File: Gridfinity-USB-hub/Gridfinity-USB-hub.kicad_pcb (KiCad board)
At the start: 4 copper layers, 40 x 40 mm, 38 parts, among them J1 USB_C_Receptacle_USB2.0_16P, J2 QWIIC, J3 USB_C_Receptacle_USB2.0_16P, J4 USB_C_Receptacle_USB2.0_16P, J5 USB_C_Receptacle_USB2.0_16P, J6 USB_C_Receptacle_USB2.0_16P, U1 CH334F, Y1 12MHz

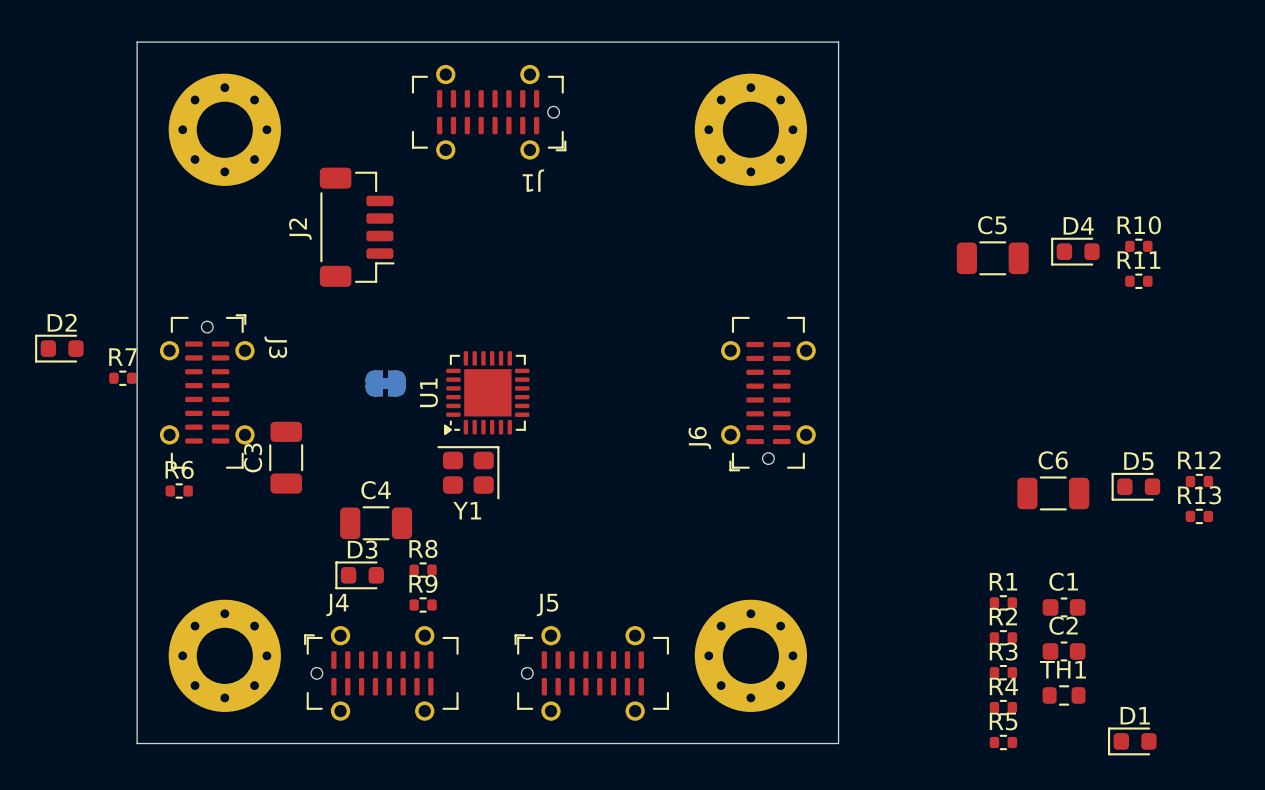
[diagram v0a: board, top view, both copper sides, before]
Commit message: USB Hub Board as order submitted on 9/6
This might get rejected by JLC for via sizes.
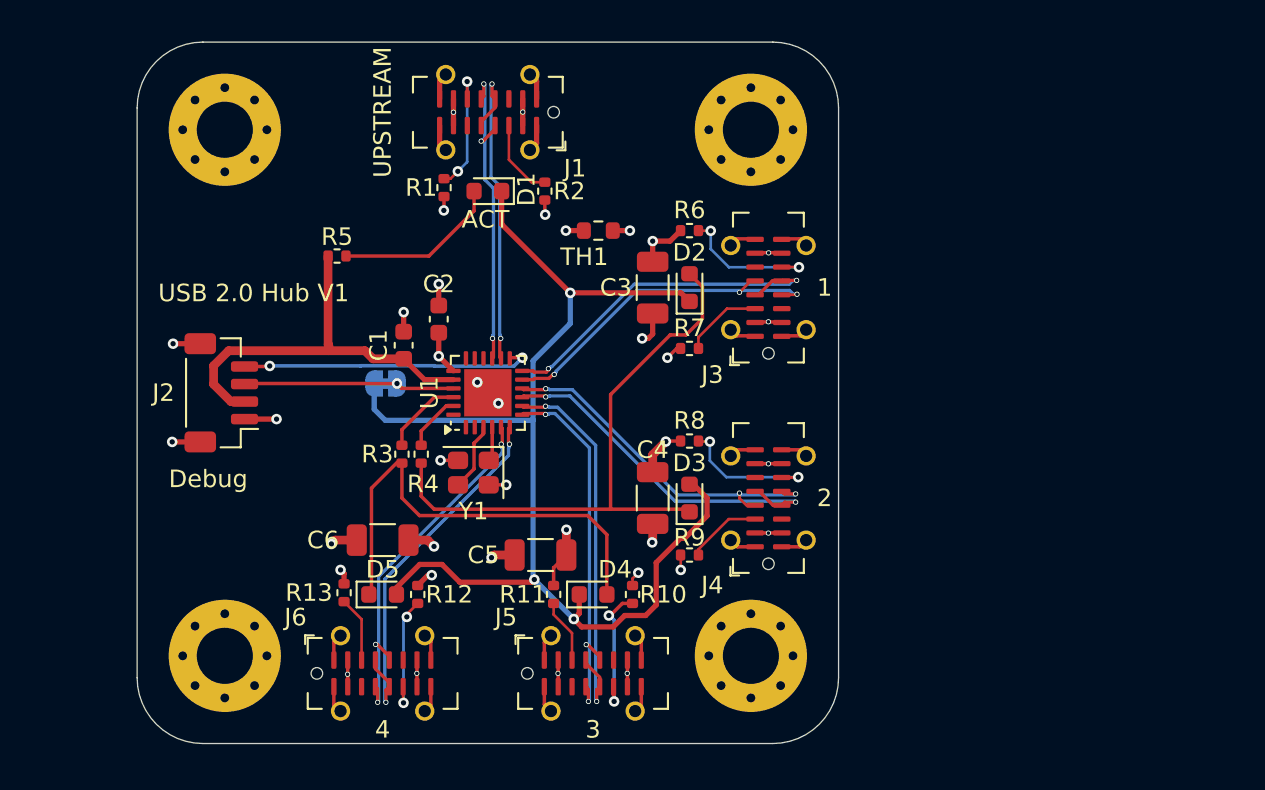
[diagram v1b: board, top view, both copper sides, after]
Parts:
- moved R13 49.0 mm to (61.8, 81.4), turned to -90 degrees
- moved D1 48.4 mm to (70.0, 58.5), turned to 180 degrees
- moved R5 47.0 mm to (61.4, 62.2)
- moved R12 45.0 mm to (66.0, 81.5), turned to -90 degrees
- moved D5 43.6 mm to (64.0, 81.5)
- moved C1 40.5 mm to (65.2, 67.3), turned to 90 degrees
- moved C2 40.4 mm to (67.2, 65.8), turned to 90 degrees
- moved R1 39.7 mm to (67.5, 58.3), turned to -90 degrees
- moved C6 38.3 mm to (64.0, 78.4), turned to 180 degrees
- moved R11 37.9 mm to (73.8, 81.5), turned to -90 degrees
- moved TH1 37.5 mm to (76.3, 60.8)
- moved R2 36.5 mm to (73.2, 58.5), turned to -90 degrees
- moved R3 36.5 mm to (65.1, 73.5), turned to -90 degrees
- moved R4 36.2 mm to (66.2, 73.5), turned to -90 degrees
- moved D2 35.9 mm to (81.5, 64.0), turned to 90 degrees
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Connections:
- J4 pad A6: /USB1.D+ -> /USB2.D+
- J4 pad A7: /USB1.D- -> /USB2.D-
- J4 pad B6: /USB1.D+ -> /USB2.D+
- J4 pad B7: /USB1.D- -> /USB2.D-
- J5 pad A6: /USB1.D+ -> /USB3.D+
- J5 pad A7: /USB1.D- -> /USB3.D-
- J5 pad B6: /USB1.D+ -> /USB3.D+
- J5 pad B7: /USB1.D- -> /USB3.D-
- J6 pad A6: /USB1.D+ -> /USB4.D+
- J6 pad A7: /USB1.D- -> /USB4.D-
- J6 pad B6: /USB1.D+ -> /USB4.D+
- J6 pad B7: /USB1.D- -> /USB4.D-
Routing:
- net /LED_COMMON: track 0.00 -> 70.6 mm, vias 0 -> 3
- net GND: track 0.00 -> 49.5 mm, vias 0 -> 15
- net /LED2: track 0.00 -> 34.0 mm
- net +5V: track 0.00 -> 28.9 mm, vias 0 -> 18
- net /LED1: track 0.00 -> 26.4 mm
- net +3V3: track 0.00 -> 23.4 mm
- net /USB3.D+: track 0.00 -> 22.6 mm, vias 0 -> 2
- net /USB3.D-: track 0.00 -> 21.5 mm, vias 0 -> 3
- net /USB4.D+: track 0.00 -> 21.5 mm, vias 0 -> 2
- net /USB4.D-: track 0.00 -> 21.1 mm, vias 0 -> 3
- net /USB2.D-: track 0.00 -> 20.9 mm, vias 0 -> 2
- net /USB1.D+: track 0.00 -> 20.6 mm, vias 0 -> 2
- net /USB2.D+: track 0.00 -> 20.4 mm, vias 0 -> 3
- net /USB1.D-: track 0.00 -> 20.0 mm, vias 0 -> 3
- net /Upstream.D-: track 0.00 -> 18.7 mm, vias 0 -> 2
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- added copper zone on In2.Cu, net VBUS
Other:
- outline, holes or cut-outs redrawn
- board text added: "1"
- board text added: "2"
- board text added: "3"
- board text added: "4"
- board text added: "ACT"
- board text added: "Debug"
- board text added: "SKEC ${ISSUE_DATE}"
- board text added: "UPSTREAM"
- board text added: "USB 2.0 Hub V${REVISION}"

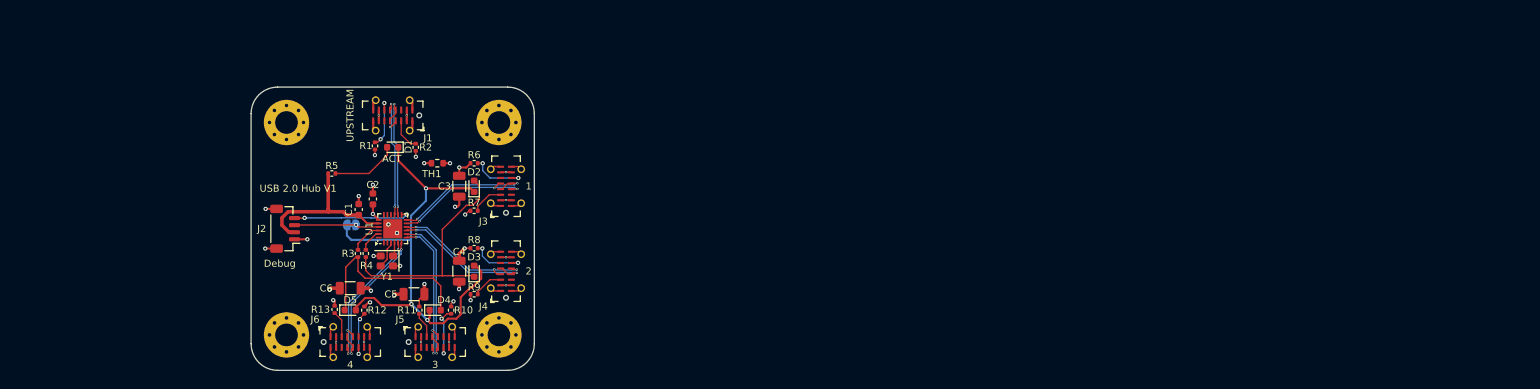
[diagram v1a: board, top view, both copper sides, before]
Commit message: Update to USB Hub to use symbol in library.  Probably some other changes as well
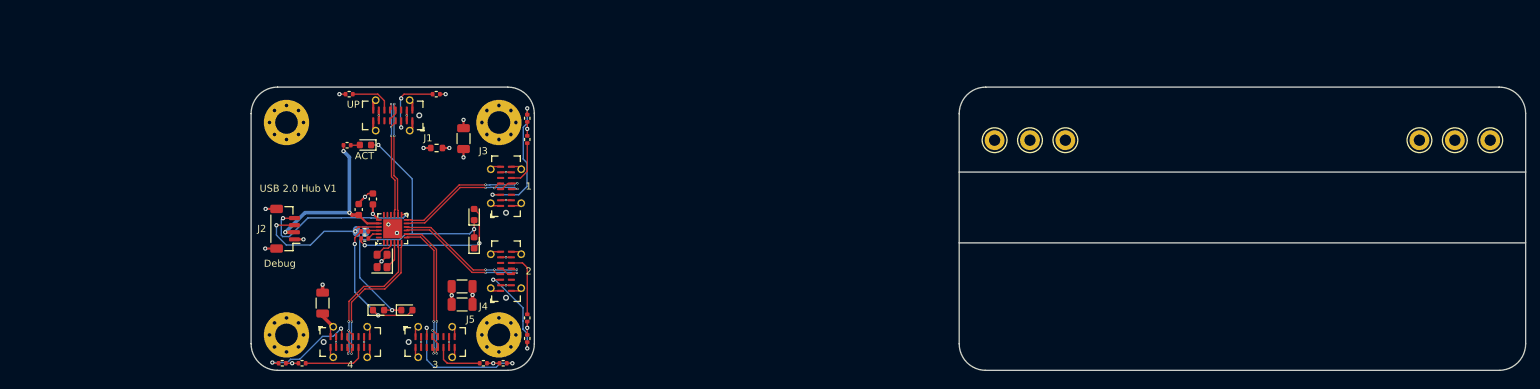
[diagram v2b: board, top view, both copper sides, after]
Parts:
- added REF**: TestPoint_Keystone_5010-5014_Multipurpose, TestPoint:TestPoint_Keystone_5010-5014_Multipurpose, F.Cu at (155.0, 57.5)
- added REF**: TestPoint_Keystone_5010-5014_Multipurpose, TestPoint:TestPoint_Keystone_5010-5014_Multipurpose, F.Cu at (220.0, 57.5)
- added REF**: TestPoint_Keystone_5010-5014_Multipurpose, TestPoint:TestPoint_Keystone_5010-5014_Multipurpose, F.Cu at (165.0, 57.5)
- added REF**: TestPoint_Keystone_5010-5014_Multipurpose, TestPoint:TestPoint_Keystone_5010-5014_Multipurpose, F.Cu at (215.0, 57.5)
- added REF**: TestPoint_Keystone_5010-5014_Multipurpose, TestPoint:TestPoint_Keystone_5010-5014_Multipurpose, F.Cu at (160.0, 57.5)
- added REF**: TestPoint_Keystone_5010-5014_Multipurpose, TestPoint:TestPoint_Keystone_5010-5014_Multipurpose, F.Cu at (225.0, 57.5)
- moved R7 15.1 mm to (89.0, 54.4), turned to 90 degrees
- moved R11 14.0 mm to (85.6, 89.0), turned to 0 degrees
- moved R8 12.4 mm to (89.0, 82.6), turned to 90 degrees
- moved R12 11.6 mm to (57.2, 89.0), turned to 0 degrees
- moved R13 10.6 mm to (54.4, 89.0), turned to 180 degrees
- moved R9 9.76 mm to (89.0, 85.5), turned to -90 degrees
- moved R10 8.77 mm to (82.8, 89.0), turned to 180 degrees
- moved R6 8.21 mm to (89.0, 57.4), turned to -90 degrees
- moved R1 8.16 mm to (63.9, 51.0), turned to 180 degrees
- moved R2 8.04 mm to (76.2, 51.0), turned to 0 degrees
- moved C5 6.95 mm to (79.8, 80.7)
- moved C3 6.75 mm to (80.0, 57.3)
- moved R5 4.54 mm to (63.6, 58.2)
- moved C6 4.43 mm to (60.1, 80.5), turned to -90 degrees
- moved D2 4.00 mm to (81.5, 68.0)
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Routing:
- net /LED_COMMON: track 70.6 -> 49.1 mm
- net Net-(J5-CC1): track 3.66 -> 19.3 mm, vias 0 -> 2
- net Net-(J3-CC1): track 4.55 -> 18.9 mm, vias 0 -> 2
- net /LED2: track 34.0 -> 23.7 mm, vias 0 -> 2
- net Net-(J6-CC1): track 3.74 -> 13.8 mm, vias 0 -> 2
- net Net-(J4-CC1): track 4.27 -> 13.8 mm, vias 0 -> 2
- net /SDA: track 12.0 -> 20.2 mm, vias 1 -> 2
- net Net-(D1-A): track 9.50 -> 1.31 mm
- net /SCL: track 16.8 -> 24.0 mm
- net /LED1: track 26.4 -> 19.8 mm, vias 0 -> 2
- net /CC1: track 4.53 -> 9.93 mm, vias 0 -> 2
- net +5V: track 28.9 -> 25.5 mm, vias 18 -> 16
- net Net-(U1-LED1): track 4.59 -> 1.53 mm
- net +3V3: track 23.4 -> 26.1 mm, vias 0 -> 3
- net Net-(J6-CC2): track 6.93 -> 9.27 mm, vias 2 -> 0
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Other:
- board size 40 x 40 mm -> 180 x 40 mm
- board text added: "2x Buss bar/power rail (Positive and Negative)"
- board text added: "5x30 Breadboard Grid"
- board text added: "Gnd"
- board text added: "Keystone 5010 (x2) & 5011 (x4) Electrically connected to the Power Rails"
- board text added: "Optional, but would fit in nicely with the Gridfinity standard"
- board text added: "Other connections to the 5x30 grid"
- board text added: "Pos"
- board text added: "UP"
- board text removed: "UPSTREAM"

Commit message: Checkpoint, changing computers
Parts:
- removed REF** (x6): TestPoint_Keystone_5010-5014_Multipurpose, TestPoint:TestPoint_Keystone_5010-5014_Multipurpose
- added C7: 10u, Capacitor_SMD:C_0603_1608Metric, F.Cu at (37.7, 69.4)
- added C8: 10u, Capacitor_SMD:C_0603_1608Metric, F.Cu at (37.7, 71.9)
- added D6: Green, LED_SMD:LED_0402_1005Metric, F.Cu at (33.7, 69.4)
- added D7: Green, LED_SMD:LED_0402_1005Metric, F.Cu at (73.0, 76.2)
- added D8: Green, LED_SMD:LED_0402_1005Metric, F.Cu at (39.8, 77.4)
- added D9: Green, LED_SMD:LED_0402_1005Metric, F.Cu at (20.1, 74.4)
- added J7: Conn_ARM_SWD_TagConnect_TC2030-NL, Connector:Tag-Connect_TC2030-IDC-NL_2x03_P1.27mm_Vertical, B.Cu at (19.7, 56.3)
- added J8: Conn_02x05_Odd_Even, Connector_PinHeader_1.27mm:PinHeader_2x05_P1.27mm_Vertical, F.Cu at (17.8, 60.4)
- added JP2: Jumper_2_Small_Bridged, Jumper:SolderJumper-2_P1.3mm_Bridged2Bar_RoundedPad1.0x1.5mm, B.Cu at (61.4, 71.5)
- added JP3: Jumper_2_Small_Open, Jumper:SolderJumper-2_P1.3mm_Open_RoundedPad1.0x1.5mm, B.Cu at (76.5, 59.1)
- added JP4: Jumper_2_Small_Open, Jumper:SolderJumper-2_P1.3mm_Open_RoundedPad1.0x1.5mm, B.Cu at (92.3, 72.8)
- added R14: 5.1k, Resistor_SMD:R_0402_1005Metric, F.Cu at (41.2, 69.1)
- added R15: 5.1k, Resistor_SMD:R_0402_1005Metric, F.Cu at (73.3, 66.8)
- added R16: 5.1k, Resistor_SMD:R_0402_1005Metric, F.Cu at (74.3, 66.8)
- added U2: CH334F, Package_DFN_QFN:QFN-24-1EP_4x4mm_P0.5mm_EP2.7x2.7mm, F.Cu at (74.3, 71.8)
- added U3: FT2232HQ, Package_DFN_QFN:QFN-64-1EP_9x9mm_P0.5mm_EP4.35x4.35mm, F.Cu at (31.5, 84.0)
- added U4: RP2040, Package_DFN_QFN:QFN-56-1EP_7x7mm_P0.4mm_EP3.2x3.2mm, F.Cu at (29.3, 59.4)
- added U5: W25Q16JVSS, Package_DFN_QFN:DFN-8-1EP_3x2mm_P0.5mm_EP1.7x1.6mm, F.Cu at (29.4, 51.2)
- added Y2: 12MHz, Crystal:Crystal_SMD_2520-4Pin_2.5x2.0mm, F.Cu at (69.0, 72.8)
- D1, D2, D3, D4, D5: footprint LED_SMD:LED_0603_1608Metric -> LED_SMD:LED_0402_1005Metric
- JP1: footprint Jumper:SolderJumper-2_P1.3mm_Bridged_RoundedPad1.0x1.5mm -> Jumper:SolderJumper-2_P1.3mm_Bridged2Bar_RoundedPad1.0x1.5mm
- moved D5 25.8 mm to (42.6, 77.0)
- moved R1 21.2 mm to (85.0, 50.8), turned to 0 degrees
- moved TH1 19.0 mm to (57.6, 62.7), turned to -90 degrees
- moved C3 15.5 mm to (80.4, 41.8)
- moved JP1 12.5 mm to (73.5, 60.8)
- moved R3 12.4 mm to (75.3, 62.2)
- moved R4 12.4 mm to (75.3, 63.2)
- moved U1 12.4 mm to (79.3, 61.8)
- moved Y1 12.4 mm to (77.8, 66.4)
- moved C1 10.7 mm to (73.7, 60.8), turned to 180 degrees
- moved C2 9.65 mm to (74.1, 59.0), turned to 180 degrees
- moved R2 6.06 mm to (82.2, 51.3)
- moved J1 6.00 mm to (76.0, 54.0)
- moved D3 4.74 mm to (86.0, 70.5), turned to 180 degrees
- moved D2 4.74 mm to (86.0, 69.5), turned to 0 degrees
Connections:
- net /CC1 renamed /Upstream/CC1
- net /CC2 renamed /Upstream/CC2
- net /LED2 renamed /LED2.K
- net /Upstream.D+ renamed /USB_Hub/Upstream.D+
- net /Upstream.D- renamed /USB_Hub/Upstream.D-
- C1 pad 1: +3V3 -> Net-(JP1-B)
- C2 pad 1: VBUS -> Net-(JP3-B)
- D1 pad 1: /LED_COMMON -> /LED_MID.A
- D2 pad 1: /LED_COMMON -> /LED_MID.A
- D3 pad 2: /LED_COMMON -> /LED_MID.A
- D4 pad 1: /LED_COMMON -> /LED_MID.A
- D4 pad 2: /LED1 -> /LED_MID.K
- D5 pad 1: /LED1 -> /LED4.K
- D5 pad 2: /LED_COMMON -> /LED4.A
- J2 pad 3: /SDA -> /Serial_comms/SDA
- J2 pad 4: /SCL -> /Serial_comms/SCL
- JP1 pad 1: /SDA -> +3V3
- JP1 pad 2: /LED_COMMON -> Net-(JP1-B)
- R3 pad 2: /LED1 -> /LED_MID.K
- U1 pad 13: /SCL -> unconnected-(U1-LED3/SCL-Pad13)
- U1 pad 17: (no net) -> unconnected-(U1-NC-Pad17)
- U1 pad 19: VBUS -> Net-(JP3-B)
- U1 pad 2: (no net) -> unconnected-(U1-NC-Pad2)
- U1 pad 20: +3V3 -> Net-(JP1-B)
- U1 pad 21: /SDA -> /LED_MID.A
- U1 pad 5: /USB4.D- -> /USB_MID.D-
- U1 pad 6: /USB4.D+ -> /USB_MID.D+
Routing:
- net /LED_COMMON: track 49.1 -> 0.00 mm, vias 3 -> 0
- net /SCL: track 24.0 -> 0.00 mm, vias 2 -> 0
- net /LED2.K: track 23.7 -> 1.18 mm, vias 2 -> 1
- net /SDA: track 20.2 -> 0.00 mm, vias 2 -> 0
- net /LED1: track 19.8 -> 0.00 mm, vias 2 -> 0
- net +3V3: track 26.1 -> 9.87 mm, vias 3 -> 1
- net /USB4.D-: track 22.5 -> 6.79 mm
- net /USB4.D+: track 23.1 -> 7.46 mm
- net /USB3.D+: track 22.7 -> 7.46 mm
- net /USB3.D-: track 21.6 -> 6.93 mm
- net /USB2.D-: track 20.9 -> 7.31 mm
- net /USB2.D+: track 20.4 -> 6.76 mm
- net /USB1.D+: track 20.6 -> 8.12 mm
- net /USB1.D-: track 20.0 -> 7.49 mm
- net /USB_Hub/Upstream.D-: track 18.7 -> 8.12 mm
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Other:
- board size 180 x 40 mm -> 40 x 40 mm
- board text removed: "2x Buss bar/power rail (Positive and Negative)"
- board text removed: "5x30 Breadboard Grid"
- board text removed: "Gnd"
- board text removed: "Keystone 5010 (x2) & 5011 (x4) Electrically connected to the Power Rails"
- board text removed: "Other connections to the 5x30 grid"
- board text removed: "Pos"
